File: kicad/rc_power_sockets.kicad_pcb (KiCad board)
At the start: 2 copper layers, 50 x 50 mm, 26 parts, among them IC1 ATTINY85, J1 PIR, J2 433MHZ, J3 433MHZ, P1 ICSP, P2 POWER_IN, Q1 NMOS, Q2 PMOS, U1 3.3V REG

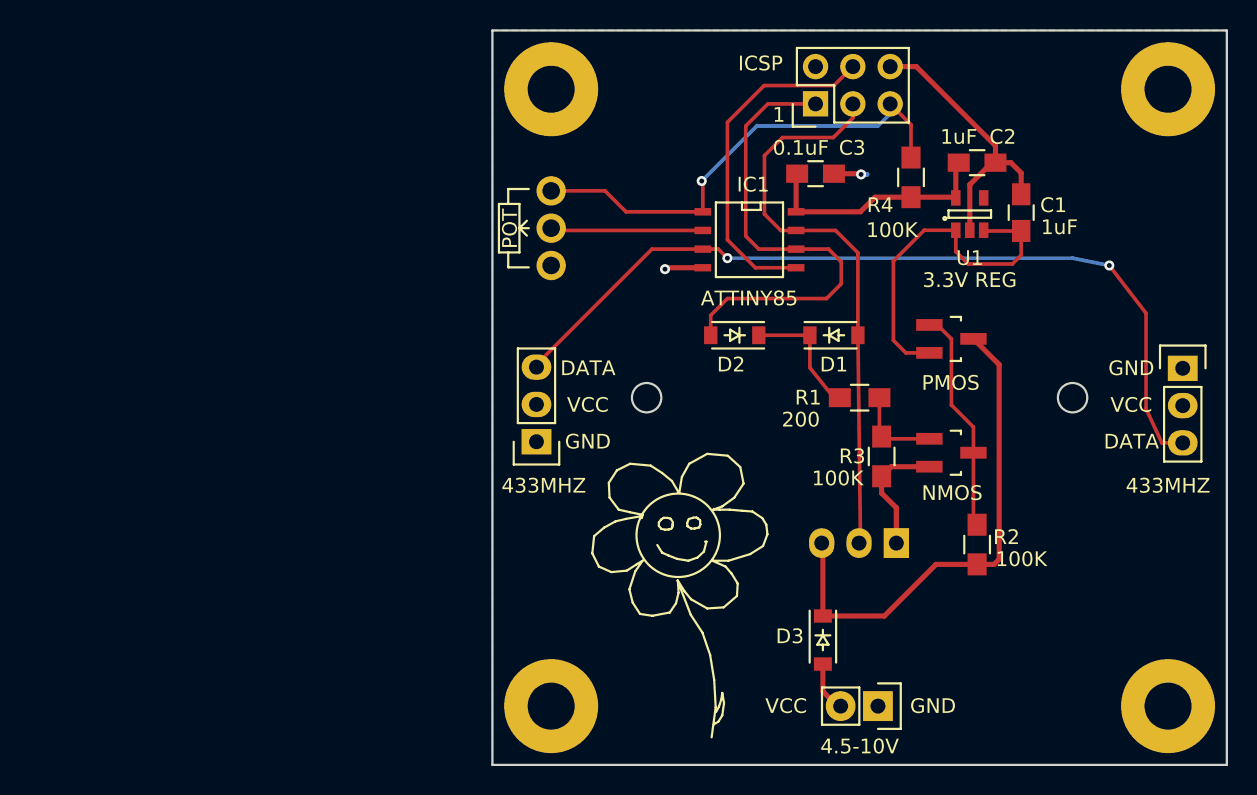
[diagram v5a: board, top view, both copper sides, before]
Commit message: Redesign with CR2032
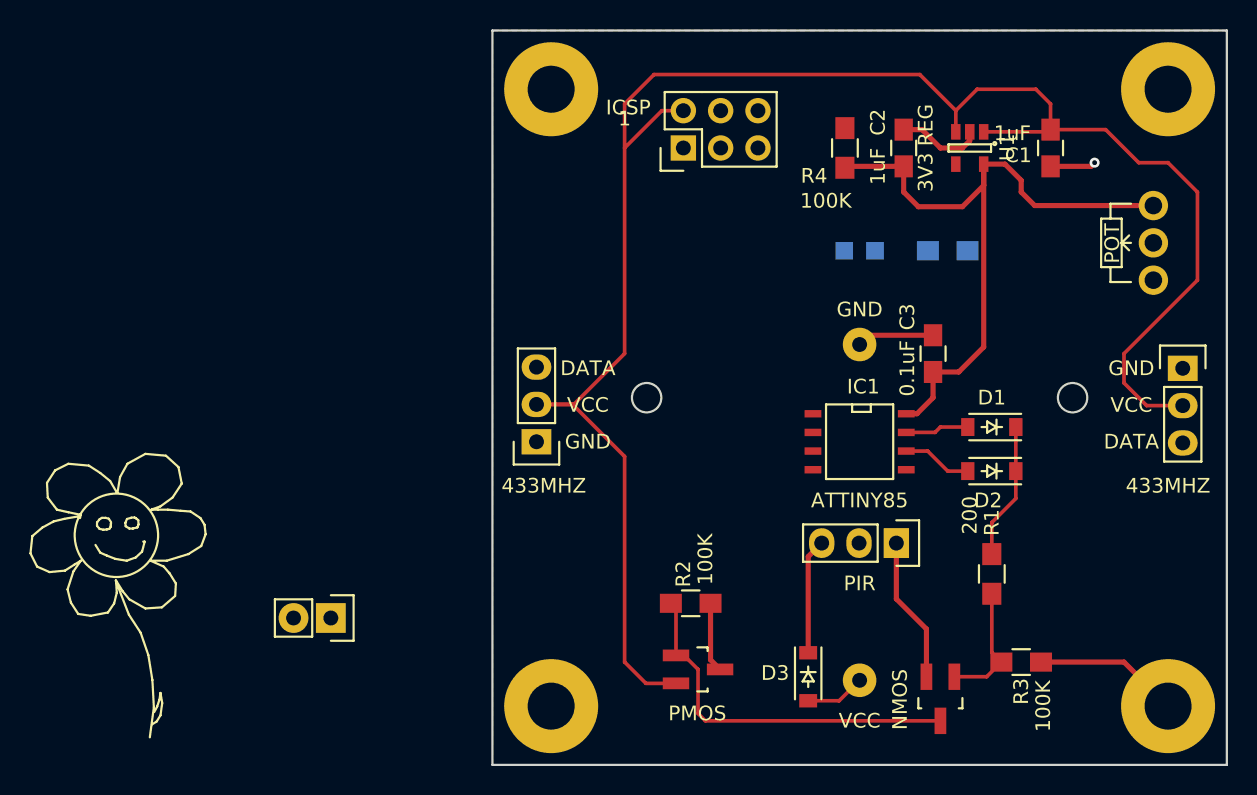
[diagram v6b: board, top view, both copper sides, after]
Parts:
- added BT1: Battery, Connect:CR2032H, B.Cu at (145.0, 89.0)
- added D4: Led, LEDs:LED_0805, B.Cu at (145.0, 75.0)
- added R5: 220, Resistors_SMD:R_0805_HandSoldering, B.Cu at (151.0, 75.0)
- J1: moved to F.Cu
- U1: value 3.3V REG -> 3V3 REG; footprint SOT-23-5 -> TO_SOT_Packages_SMD:SOT-23-5
- moved REF** 41.3 mm to (186.0, 74.0)
- moved RV1 41.0 mm to (165.0, 77.0)
- moved REF** 38.2 mm to (94.0, 87.5)
- moved P2 37.7 mm to (109.0, 100.0)
- moved Q2 28.4 mm to (134.0, 103.5)
- moved R2 19.9 mm to (133.5, 99.0), turned to 180 degrees
- moved D2 19.8 mm to (154.0, 90.0)
- moved R3 16.9 mm to (156.0, 103.0), turned to 0 degrees
- moved Q1 16.8 mm to (150.5, 105.5), turned to 180 degrees
- moved IC1 15.7 mm to (145.0, 88.0)
- moved R1 15.0 mm to (154.0, 97.0), turned to 90 degrees
- moved C3 14.6 mm to (150.0, 82.0), turned to 90 degrees
- moved D1 12.4 mm to (154.0, 87.0), turned to 180 degrees
- moved P1 9.49 mm to (133.0, 68.0)
- moved C2 5.10 mm to (148.0, 68.0), turned to 90 degrees
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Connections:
- D3 pad 2: VCC -> Net-(BT1-Pad1)
- RV1 pad 3: /RESET -> /3.3v
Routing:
- net /SWITCH_POWER: track 24.0 -> 126.2 mm
- net /RADIO_DATA: track 57.9 -> 0.17 mm, vias 2 -> 0
- net /SCK: track 39.6 -> 4.49 mm
- net /RESET: track 32.7 -> 0.00 mm, vias 1 -> 0
- net /3.3v: track 16.4 -> 47.9 mm
- net /MISO: track 32.7 -> 4.76 mm
- net /MOSI: track 23.6 -> 0.00 mm
- net /POWER: track 34.4 -> 12.8 mm
- net /ADC3: track 10.4 -> 0.00 mm
- net /PBASE: track 15.3 -> 25.3 mm
- net Net-(BT1-Pad1): track 0.00 -> 4.08 mm
- net VCC: track 3.49 -> 0.00 mm
- net /NBASE: track 6.02 -> 8.53 mm
- net GND: track 33.1 -> 34.0 mm, vias 2 -> 1

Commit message: Two cell batteries for 6V
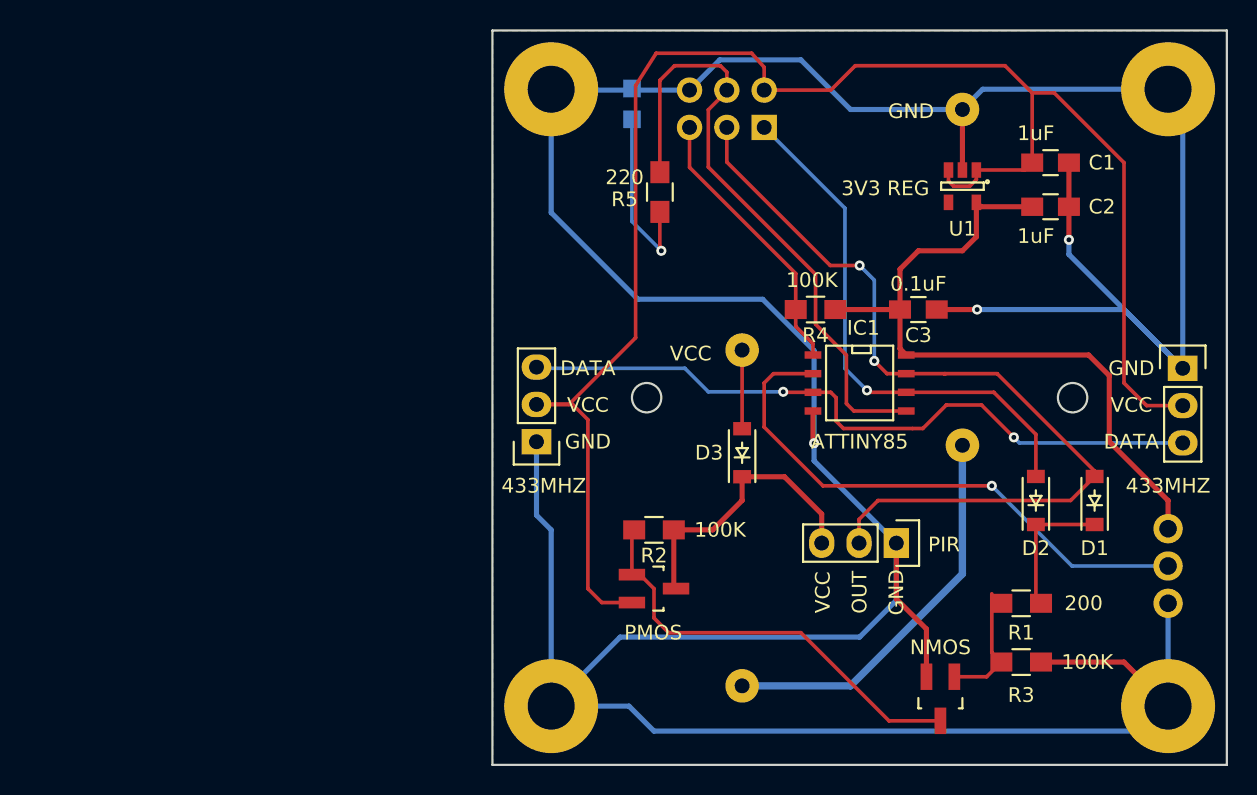
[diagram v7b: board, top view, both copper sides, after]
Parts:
- removed P2: POWER_IN, Pin_Headers:Pin_Header_Straight_1x02
- removed the REF** at (94.0, 87.5)
- added BT2: Battery, Connect:CR2032H, B.Cu at (152.0, 73.0)
- P1, RV1: moved to B.Cu
- R5: moved to F.Cu
- moved REF** 30.6 mm to (159.0, 88.5)
- moved RV1 22.0 mm to (166.0, 99.0), turned to 0 degrees
- moved R5 20.0 mm to (131.4, 71.0), turned to 270 degrees
- moved D4 18.4 mm to (129.5, 65.0), turned to 270 degrees
- moved D3 15.9 mm to (137.0, 88.8), turned to 90 degrees
- moved BT1 11.3 mm to (137.0, 97.0), turned to 90 degrees
- moved R4 11.2 mm to (142.0, 79.0), turned to 0 degrees
- moved C2 10.8 mm to (158.0, 72.0), turned to 0 degrees
- moved D1 8.60 mm to (161.0, 92.0), turned to 90 degrees
- moved Q2 6.26 mm to (131.0, 98.0)
- moved P1 5.68 mm to (138.5, 66.6)
- moved R2 5.59 mm to (131.0, 94.0)
- moved IC1 4.00 mm to (145.0, 84.0)
- moved D2 3.61 mm to (157.0, 92.0), turned to 90 degrees
- moved C3 3.16 mm to (149.0, 79.0), turned to 0 degrees
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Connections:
- net Net-(BT1-Pad1) renamed /VCC
- BT1 pad 2: GND -> /BATT
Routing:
- net GND: track 34.0 -> 271.4 mm, vias 1 -> 3
- net /SCK: track 4.49 -> 58.8 mm, vias 0 -> 2
- net /RADIO_DATA: track 0.17 -> 48.4 mm, vias 0 -> 2
- net /MOSI: track 0.00 -> 43.5 mm
- net /ADC3: track 0.00 -> 38.0 mm, vias 0 -> 1
- net /MISO: track 4.76 -> 36.4 mm, vias 0 -> 1
- net /BATT: track 0.00 -> 26.9 mm
- net /RESET: track 0.00 -> 19.0 mm
- net Net-(D4-Pad2): track 0.00 -> 12.5 mm, vias 0 -> 1
- net /SWITCH_POWER: track 126.2 -> 116.5 mm
- net /POWER: track 12.8 -> 19.7 mm
- net /PBASE: track 25.3 -> 29.4 mm
- net /3.3v: track 47.9 -> 49.3 mm
- net /VCC: track 4.08 -> 5.35 mm
- net /NBASE_ON: track 9.33 -> 10.0 mm
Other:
- net class Battery added: clearance 0.6, trace_width 0.5, via_dia 0.6858, via_drill 0.3302

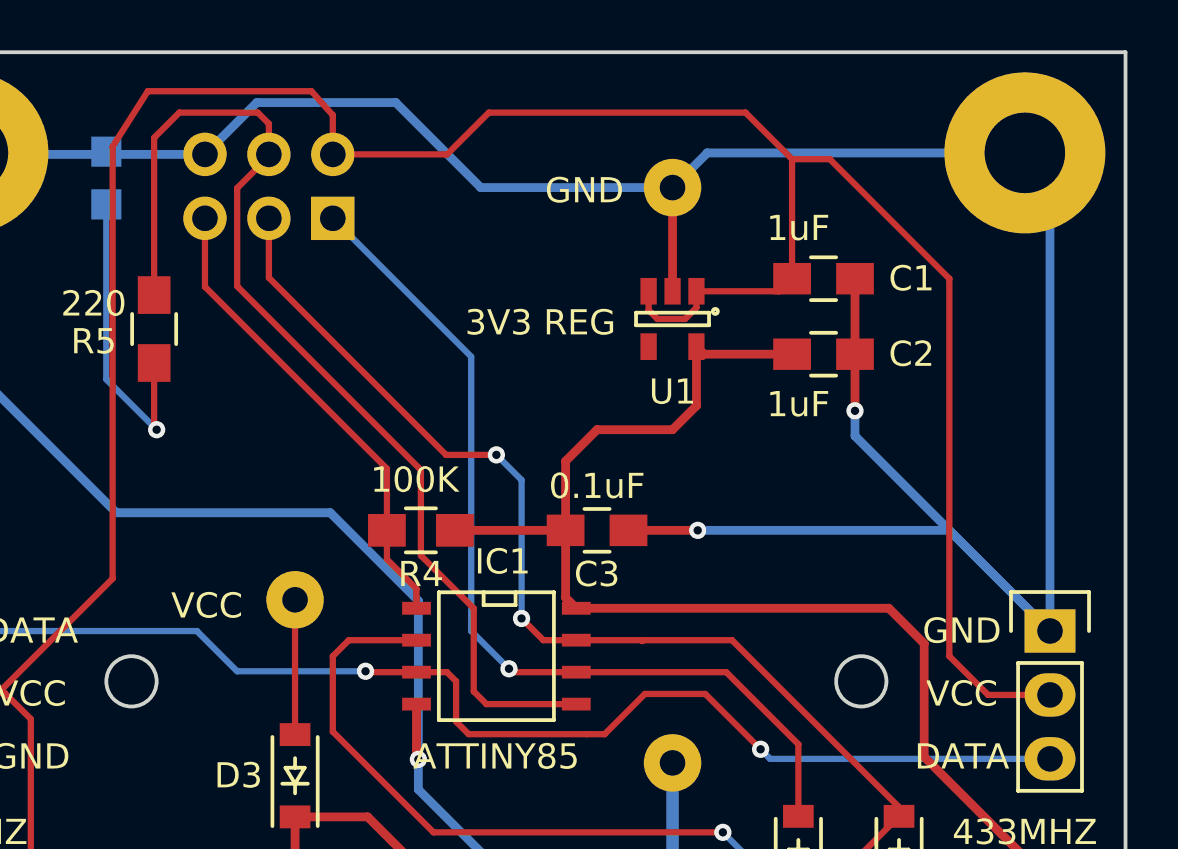
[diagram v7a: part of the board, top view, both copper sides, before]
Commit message: MCP1755S 3v3 voltage regulator
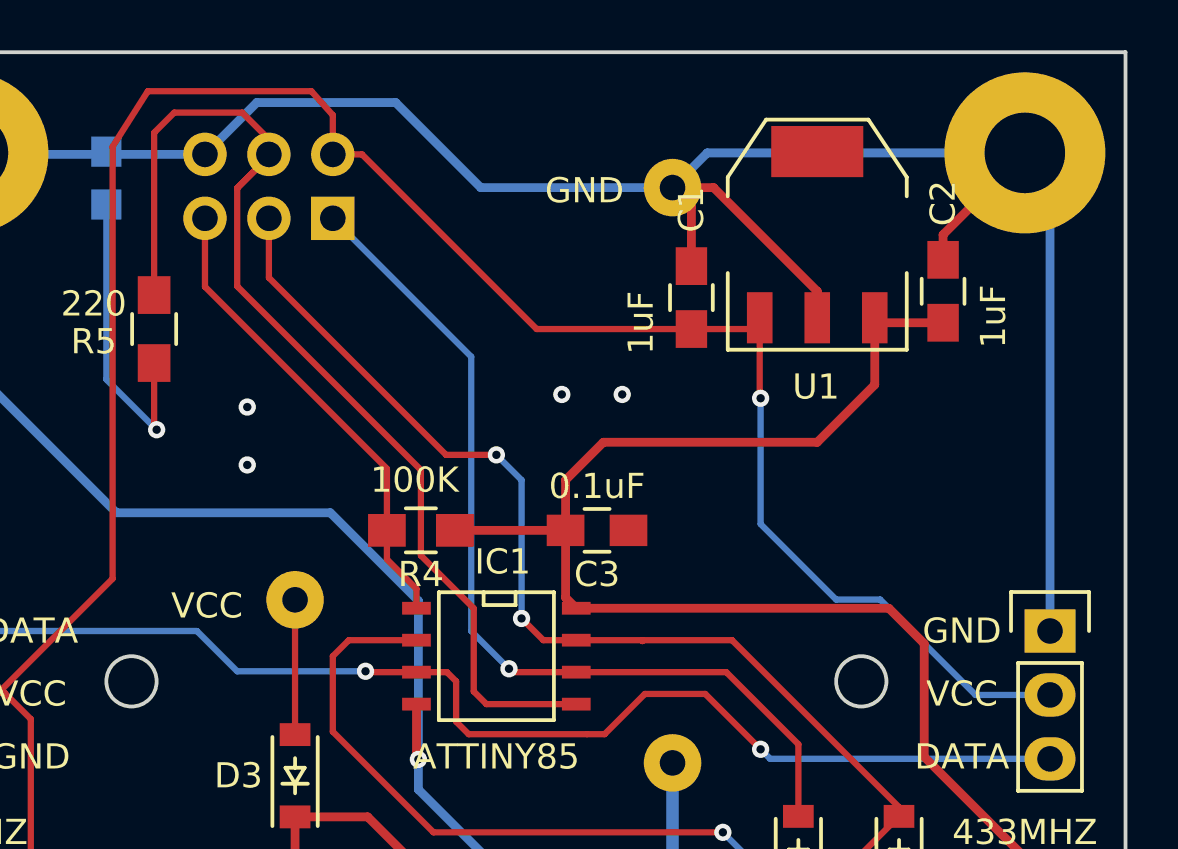
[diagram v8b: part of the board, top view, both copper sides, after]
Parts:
- U1: footprint TO_SOT_Packages_SMD:SOT-23-5 -> TO_SOT_Packages_SMD:SOT-223
- moved U1 6.65 mm to (157.8, 67.2), turned to 0 degrees
- moved C2 5.37 mm to (162.8, 69.5), turned to 90 degrees
- moved C1 5.30 mm to (152.8, 69.8), turned to 90 degrees
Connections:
- U1 pad 3: /SWITCH_POWER -> /3.3v
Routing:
- net GND: track 271.4 -> 249.2 mm, vias 3 -> 5
- net /SWITCH_POWER: track 116.5 -> 99.1 mm, vias 0 -> 1
- net /3.3v: track 49.3 -> 55.5 mm
- net /MOSI: track 43.5 -> 44.2 mm
- added copper zone on F.Cu, net GND
- removed copper zone on F.Cu, net /SWITCH_POWER
